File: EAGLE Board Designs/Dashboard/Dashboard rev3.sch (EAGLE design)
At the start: 91 parts, among them J2 CONNECTOR-8_NF_S_RA_BLACK, J3 CONNECTOR-CAN_NF_S_RA_BLACK, J4 CONNECTOR-AVR-ISP_2X05_SMD_, K1 CPC1002N, Q1 TRANSISTOR_N_MOS__PMV15ENEA, Q2 TRANSISTOR_N_MOS__PMV15ENEA, Q3 TRANSISTOR_N_MOS__PMV15ENEA, Q4 TRANSISTOR_N_MOS__PMV15ENEA, Q5 TRANSISTOR_N_MOS__PMV15ENEA, Q6 TRANSISTOR_N_MOS__PMV15ENEA, U1 ATMEGA328P-AU, U2 TCAN1051HQV-Q1, U3 MCP2515, U4 MCP23S17, U5 CONVERTER_DC/DC_12V-5V, U6 RE46C100, X1 CRYSTAL16MHZ, X2 CRYSTAL16MHZ, X7 CONNECTOR-8NANO-FIT_RIGHT_ANG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

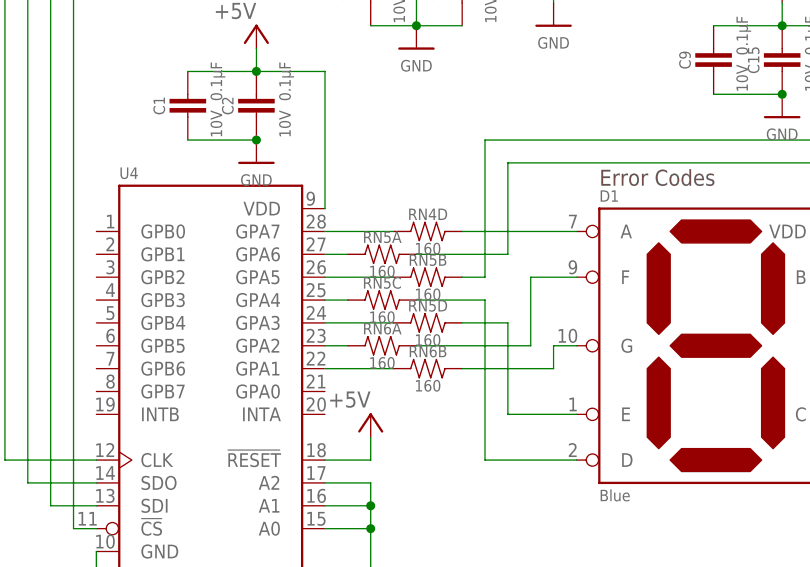
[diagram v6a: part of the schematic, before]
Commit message: Simplified resistor network for LED 7 Seg
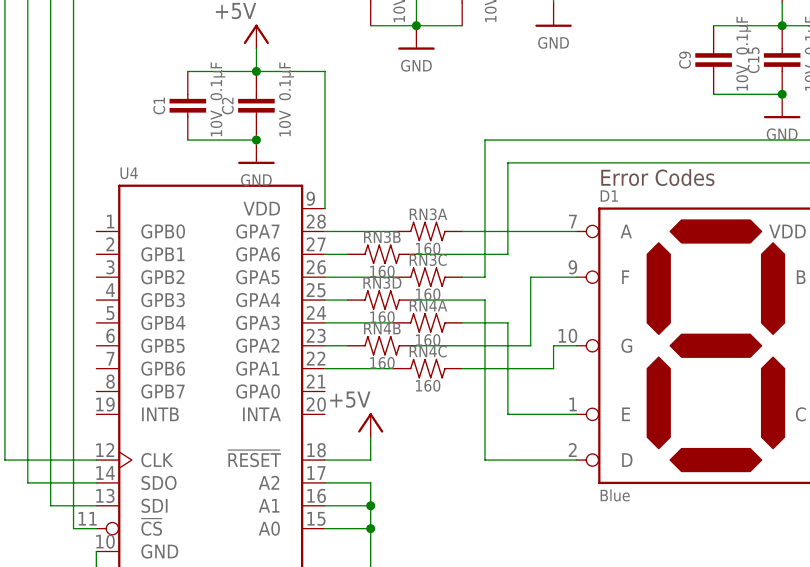
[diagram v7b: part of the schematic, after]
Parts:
- removed RN5, RN6: RESISTOR_NETWORK_4_160, HyTechDevices:RESISTOR_NETWORK_4_160
- added RN3: RESISTOR_NETWORK_4_160, HyTechDevices:RESISTOR_NETWORK_4_160
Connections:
- net A2: now also RN3A.1; no longer RN4D.1
- net B2: now also RN3B.1; no longer RN5A.1
- net C2: now also RN3C.1; no longer RN5B.1
- net D2: now also RN3D.1; no longer RN5C.1
- net E2: now also RN4A.1; no longer RN5D.1
- net F2: now also RN4B.1; no longer RN6A.1
- net G2: now also RN4C.1; no longer RN6B.1
- net N$13: now also RN3A.2; no longer RN4D.2
- net N$14: now also RN3B.2; no longer RN5A.2
- net N$15: now also RN3C.2; no longer RN5B.2
- net N$16: now also RN4C.2; no longer RN6B.2
- net N$17: now also RN4B.2; no longer RN6A.2
- net N$18: now also RN4A.2; no longer RN5D.2
- net N$19: now also RN3D.2; no longer RN5C.2
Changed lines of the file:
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@@
 <part name="P20" library="HyTechSupplies" deviceset="GND" device=""/>
 <part name="FRAME1" library="HyTechFrames" deviceset="FRAME" device=""/>
-<part name="RN4" library="HyTechDevices" deviceset="RESISTOR_NETWORK_4_*" device="" technology="160"/>
-<part name="RN5" library="HyTechDevices" deviceset="RESISTOR_NETWORK_4_*" device="" technology="160"/>
-<part name="RN6" library="HyTechDevices" deviceset="RESISTOR_NETWORK_4_*" device="" technology="160"/>
 <part name="P+5" library="supply1" library_urn="urn:adsk.eagle:library:371" deviceset="+5V" device=""/>
 <part name="U2" library="HyTechDevices" deviceset="TCAN1051*V-Q1" device="" technology="HQ"/>
@@
 <part name="P24" library="HyTechSupplies" deviceset="GND" device=""/>
 <part name="R16" library="HyTechDevices" deviceset="RESISTOR_?_*" device="0603" technology="10K"/>
+<part name="RN3" library="HyTechDevices" deviceset="RESISTOR_NETWORK_4_*" device="" technology="160"/>
+<part name="RN4" library="HyTechDevices" deviceset="RESISTOR_NETWORK_4_*" device="" technology="160"/>
 </parts>
 <sheets>
@@
 <attribute name="DESCRIPTION_2" x="176.53" y="10.16" size="2.54" layer="95"/>
 </instance>
-<instance part="RN4" gate="D" x="218.44" y="116.84" smashed="yes">
-<attribute name="NAME" x="217.17" y="118.11" size="1.27" layer="95" align="bottom-center"/>
-<attribute name="RESISTANCE" x="217.17" y="115.57" size="1.27" layer="96" align="top-center"/>
-</instance>
-<instance part="RN5" gate="A" x="213.36" y="114.3" smashed="yes">
-<attribute name="NAME" x="212.09" y="115.57" size="1.27" layer="95" align="bottom-center"/>
-<attribute name="RESISTANCE" x="212.09" y="113.03" size="1.27" layer="96" align="top-center"/>
-</instance>
-<instance part="RN5" gate="B" x="218.44" y="111.76" smashed="yes">
-<attribute name="NAME" x="217.17" y="113.03" size="1.27" layer="95" align="bottom-center"/>
-<attribute name="RESISTANCE" x="217.17" y="110.49" size="1.27" layer="96" align="top-center"/>
-</instance>
-<instance part="RN5" gate="C" x="213.36" y="109.22" smashed="yes">
-<attribute name="NAME" x="212.09" y="110.49" size="1.27" layer="95" align="bottom-center"/>
-<attribute name="RESISTANCE" x="212.09" y="107.95" size="1.27" layer="96" align="top-center"/>
-</instance>
-<instance part="RN5" gate="D" x="218.44" y="106.68" smashed="yes">
-<attribute name="NAME" x="217.17" y="107.95" size="1.27" layer="95" align="bottom-center"/>
-<attribute name="RESISTANCE" x="217.17" y="105.41" size="1.27" layer="96" align="top-center"/>
-</instance>
-<instance part="RN6" gate="A" x="213.36" y="104.14" smashed="yes">
-<attribute name="NAME" x="212.09" y="105.41" size="1.27" layer="95" align="bottom-center"/>
-<attribute name="RESISTANCE" x="212.09" y="102.87" size="1.27" layer="96" align="top-center"/>
-</instance>
-<instance part="RN6" gate="B" x="218.44" y="101.6" smashed="yes">
-<attribute name="NAME" x="217.17" y="102.87" size="1.27" layer="95" align="bottom-center"/>
-<attribute name="RESISTANCE" x="217.17" y="100.33" size="1.27" layer="96" align="top-center"/>
-</instance>
 <instance part="P+5" gate="1" x="210.82" y="96.52" smashed="yes">
 <attribute name="VALUE" x="210.82" y="99.06" size="1.778" layer="96" rot="R180"/>
@@
 <attribute name="NAME" x="52.07" y="19.05" size="1.27" layer="95" align="bottom-center"/>
 <attribute name="RESISTANCE" x="52.07" y="16.51" size="1.27" layer="96" align="top-center"/>
+</instance>
+<instance part="RN3" gate="A" x="218.44" y="116.84" smashed="yes">
+<attribute name="NAME" x="217.17" y="118.11" size="1.27" layer="95" align="bottom-center"/>
+<attribute name="RESISTANCE" x="217.17" y="115.57" size="1.27" layer="96" align="top-center"/>
+</instance>
+<instance part="RN3" gate="B" x="213.36" y="114.3" smashed="yes">
+<attribute name="NAME" x="212.09" y="115.57" size="1.27" layer="95" align="bottom-center"/>
+<attribute name="RESISTANCE" x="212.09" y="113.03" size="1.27" layer="96" align="top-center"/>
+</instance>
+<instance part="RN3" gate="C" x="218.44" y="111.76" smashed="yes">
+<attribute name="NAME" x="217.17" y="113.03" size="1.27" layer="95" align="bottom-center"/>
+<attribute name="RESISTANCE" x="217.17" y="110.49" size="1.27" layer="96" align="top-center"/>
+</instance>
+<instance part="RN3" gate="D" x="213.36" y="109.22" smashed="yes">
+<attribute name="NAME" x="212.09" y="110.49" size="1.27" layer="95" align="bottom-center"/>
+<attribute name="RESISTANCE" x="212.09" y="107.95" size="1.27" layer="96" align="top-center"/>
+</instance>
+<instance part="RN4" gate="A" x="218.44" y="106.68" smashed="yes">
+<attribute name="NAME" x="217.17" y="107.95" size="1.27" layer="95" align="bottom-center"/>
+<attribute name="RESISTANCE" x="217.17" y="105.41" size="1.27" layer="96" align="top-center"/>
+</instance>
+<instance part="RN4" gate="B" x="213.36" y="104.14" smashed="yes">
+<attribute name="NAME" x="212.09" y="105.41" size="1.27" layer="95" align="bottom-center"/>
+<attribute name="RESISTANCE" x="212.09" y="102.87" size="1.27" layer="96" align="top-center"/>
+</instance>
+<instance part="RN4" gate="C" x="218.44" y="101.6" smashed="yes">
+<attribute name="NAME" x="217.17" y="102.87" size="1.27" layer="95" align="bottom-center"/>
+<attribute name="RESISTANCE" x="217.17" y="100.33" size="1.27" layer="96" align="top-center"/>
 </instance>
 </instances>
@@
 <segment>
 <wire x1="205.74" y1="116.84" x2="213.36" y2="116.84" width="0.1524" layer="91"/>
-<pinref part="RN4" gate="D" pin="1"/>
 <pinref part="U4" gate="G$1" pin="GPA7"/>
+<pinref part="RN3" gate="A" pin="1"/>
 </segment>
 </net>
@@
 <segment>
 <wire x1="205.74" y1="114.3" x2="208.28" y2="114.3" width="0.1524" layer="91"/>
-<pinref part="RN5" gate="A" pin="1"/>
 <pinref part="U4" gate="G$1" pin="GPA6"/>
+<pinref part="RN3" gate="B" pin="1"/>
 </segment>
 </net>
@@
 <segment>
 <wire x1="205.74" y1="111.76" x2="213.36" y2="111.76" width="0.1524" layer="91"/>
-<pinref part="RN5" gate="B" pin="1"/>
 <pinref part="U4" gate="G$1" pin="GPA5"/>
+<pinref part="RN3" gate="C" pin="1"/>
 </segment>
 </net>
@@
 <segment>
 <wire x1="205.74" y1="109.22" x2="208.28" y2="109.22" width="0.1524" layer="91"/>
-<pinref part="RN5" gate="C" pin="1"/>
 <pinref part="U4" gate="G$1" pin="GPA4"/>
+<pinref part="RN3" gate="D" pin="1"/>
 </segment>
 </net>
@@
 <segment>
 <wire x1="205.74" y1="106.68" x2="213.36" y2="106.68" width="0.1524" layer="91"/>
-<pinref part="RN5" gate="D" pin="1"/>
 <pinref part="U4" gate="G$1" pin="GPA3"/>
+<pinref part="RN4" gate="A" pin="1"/>
 </segment>
 </net>
@@
 <segment>
 <wire x1="205.74" y1="104.14" x2="208.28" y2="104.14" width="0.1524" layer="91"/>
-<pinref part="RN6" gate="A" pin="1"/>
 <pinref part="U4" gate="G$1" pin="GPA2"/>
+<pinref part="RN4" gate="B" pin="1"/>
 </segment>
 </net>
@@
 <segment>
 <wire x1="205.74" y1="101.6" x2="213.36" y2="101.6" width="0.1524" layer="91"/>
-<pinref part="RN6" gate="B" pin="1"/>
 <pinref part="U4" gate="G$1" pin="GPA1"/>
+<pinref part="RN4" gate="C" pin="1"/>
 </segment>
 </net>
@@
 <net name="N$13" class="0">
 <segment>
-<pinref part="RN4" gate="D" pin="2"/>
 <pinref part="D1" gate="G$1" pin="A"/>
 <wire x1="220.98" y1="116.84" x2="233.68" y2="116.84" width="0.1524" layer="91"/>
+<pinref part="RN3" gate="A" pin="2"/>
 </segment>
 </net>
 <net name="N$14" class="0">
 <segment>
-<pinref part="RN5" gate="A" pin="2"/>
 <wire x1="215.9" y1="114.3" x2="226.06" y2="114.3" width="0.1524" layer="91"/>
 <wire x1="226.06" y1="114.3" x2="226.06" y2="124.46" width="0.1524" layer="91"/>
@@
 <pinref part="D1" gate="G$1" pin="B"/>
 <wire x1="266.7" y1="111.76" x2="264.16" y2="111.76" width="0.1524" layer="91"/>
+<pinref part="RN3" gate="B" pin="2"/>
 </segment>
 </net>
 <net name="N$15" class="0">
 <segment>
-<pinref part="RN5" gate="B" pin="2"/>
 <wire x1="220.98" y1="111.76" x2="223.52" y2="111.76" width="0.1524" layer="91"/>
 <wire x1="223.52" y1="111.76" x2="223.52" y2="127" width="0.1524" layer="91"/>
@@
 <wire x1="269.24" y1="127" x2="269.24" y2="96.52" width="0.1524" layer="91"/>
 <wire x1="269.24" y1="96.52" x2="264.16" y2="96.52" width="0.1524" layer="91"/>
+<pinref part="RN3" gate="C" pin="2"/>
 </segment>
 </net>
 <net name="N$16" class="0">
 <segment>
-<pinref part="RN6" gate="B" pin="2"/>
 <wire x1="220.98" y1="101.6" x2="231.14" y2="101.6" width="0.1524" layer="91"/>
 <pinref part="D1" gate="G$1" pin="G"/>
 <wire x1="231.14" y1="101.6" x2="231.14" y2="104.14" width="0.1524" layer="91"/>
 <wire x1="231.14" y1="104.14" x2="233.68" y2="104.14" width="0.1524" layer="91"/>
+<pinref part="RN4" gate="C" pin="2"/>
 </segment>
 </net>
 <net name="N$17" class="0">
 <segment>
-<pinref part="RN6" gate="A" pin="2"/>
 <wire x1="215.9" y1="104.14" x2="228.6" y2="104.14" width="0.1524" layer="91"/>
 <wire x1="228.6" y1="104.14" x2="228.6" y2="111.76" width="0.1524" layer="91"/>
 <pinref part="D1" gate="G$1" pin="F"/>
 <wire x1="228.6" y1="111.76" x2="233.68" y2="111.76" width="0.1524" layer="91"/>
+<pinref part="RN4" gate="B" pin="2"/>
 </segment>
 </net>
 <net name="N$18" class="0">
 <segment>
-<pinref part="RN5" gate="D" pin="2"/>
 <wire x1="220.98" y1="106.68" x2="226.06" y2="106.68" width="0.1524" layer="91"/>
 <wire x1="226.06" y1="106.68" x2="226.06" y2="96.52" width="0.1524" layer="91"/>
 <pinref part="D1" gate="G$1" pin="E"/>
 <wire x1="226.06" y1="96.52" x2="233.68" y2="96.52" width="0.1524" layer="91"/>
+<pinref part="RN4" gate="A" pin="2"/>
 </segment>
 </net>
 <net name="N$19" class="0">
 <segment>
-<pinref part="RN5" gate="C" pin="2"/>
 <wire x1="215.9" y1="109.22" x2="223.52" y2="109.22" width="0.1524" layer="91"/>
 <pinref part="D1" gate="G$1" pin="D"/>
 <wire x1="223.52" y1="109.22" x2="223.52" y2="91.44" width="0.1524" layer="91"/>
 <wire x1="223.52" y1="91.44" x2="233.68" y2="91.44" width="0.1524" layer="91"/>
-</segment>
-</net>
+<pinref part="RN3" gate="D" pin="2"/>
+</segment>
+</net>

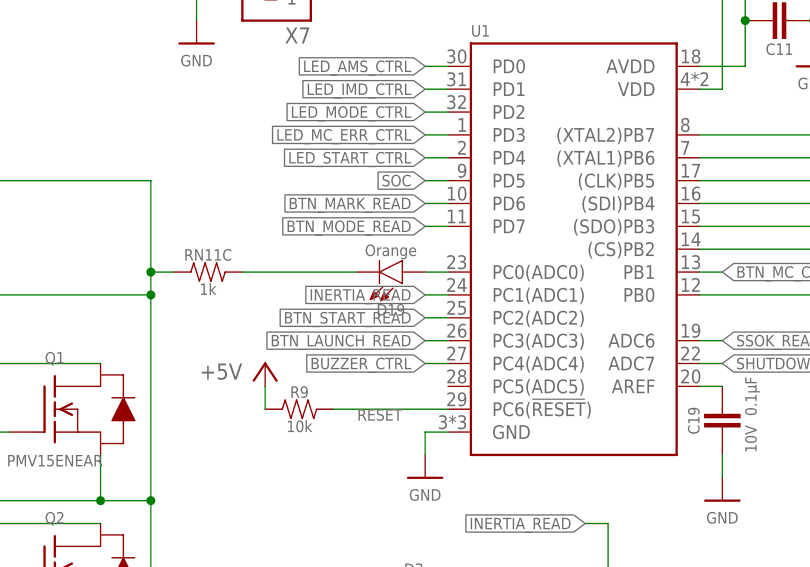
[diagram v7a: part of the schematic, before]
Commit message: Moved SOC to pin 28
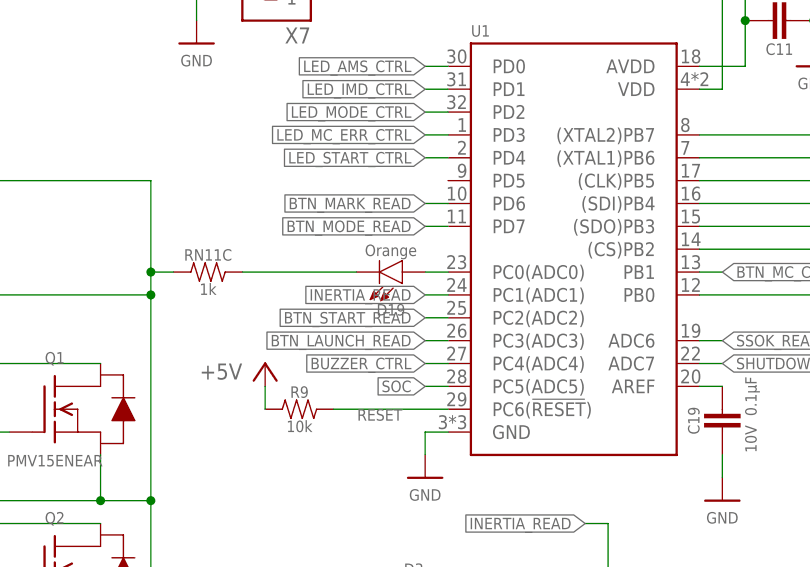
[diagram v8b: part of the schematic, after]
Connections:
- net SOC: now also U1.PC5(ADC5); no longer U1.PD5
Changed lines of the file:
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@@
 </segment>
 <segment>
-<wire x1="106.68" y1="157.48" x2="104.14" y2="157.48" width="0.1524" layer="91"/>
-<label x="104.14" y="157.48" size="1.27" layer="95" rot="MR0" xref="yes"/>
-<pinref part="U1" gate="G$1" pin="PD5"/>
+<label x="104.14" y="134.62" size="1.27" layer="95" rot="MR0" xref="yes"/>
+<pinref part="U1" gate="G$1" pin="PC5(ADC5)"/>
+<wire x1="106.68" y1="134.62" x2="104.14" y2="134.62" width="0.1524" layer="91"/>
 </segment>
 </net>
